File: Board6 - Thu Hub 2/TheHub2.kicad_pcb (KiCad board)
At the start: 2 copper layers, 53.3 x 127 mm, 31 parts, among them J1 12V Power, J2 SERVO, J3 I2C, U1 BNO055-Breakout, U2 FeatherM0, U3 RFM95-Breakout, U4 AZ1117-3.3, U5 L7806, U6 GT-U7_GPS, U7 MPL3115A2-Breakout

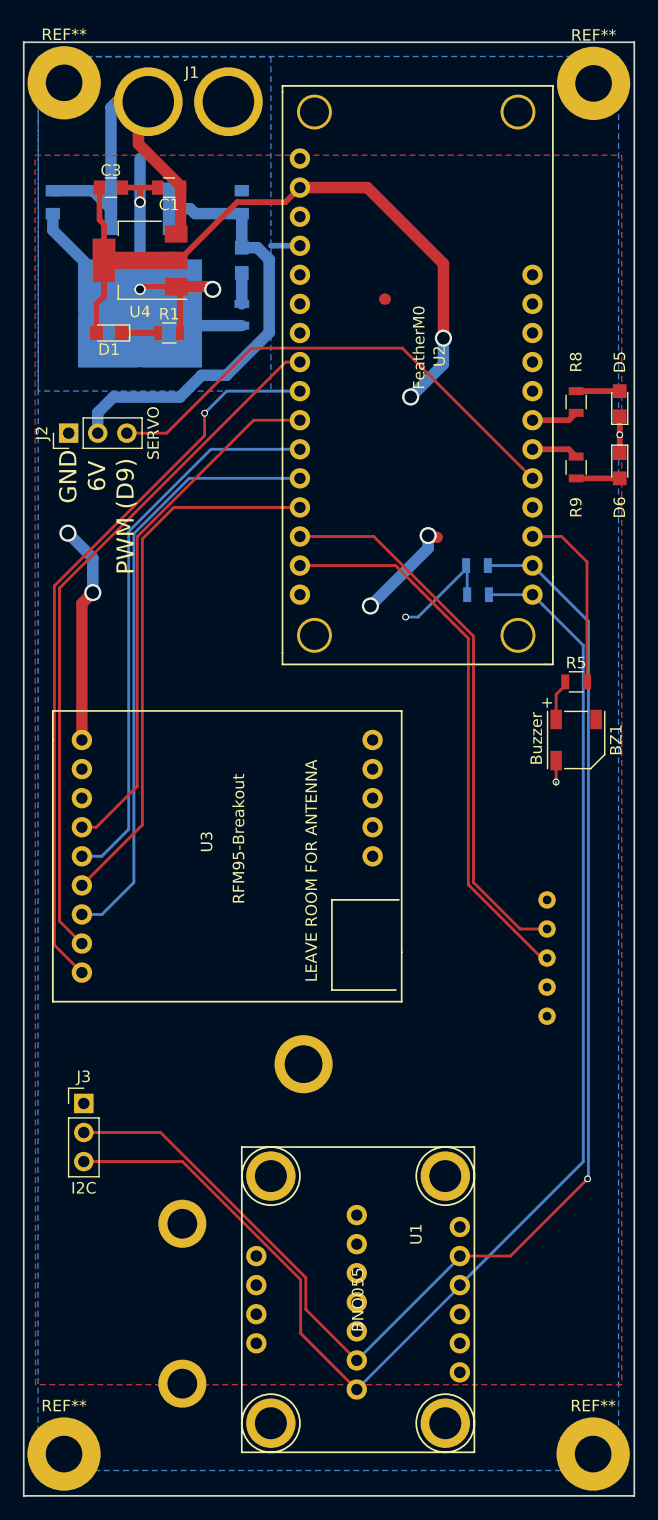
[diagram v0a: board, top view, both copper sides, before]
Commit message: For Hub2: add servo2 and GPS changed to breakout for MAX M8Q
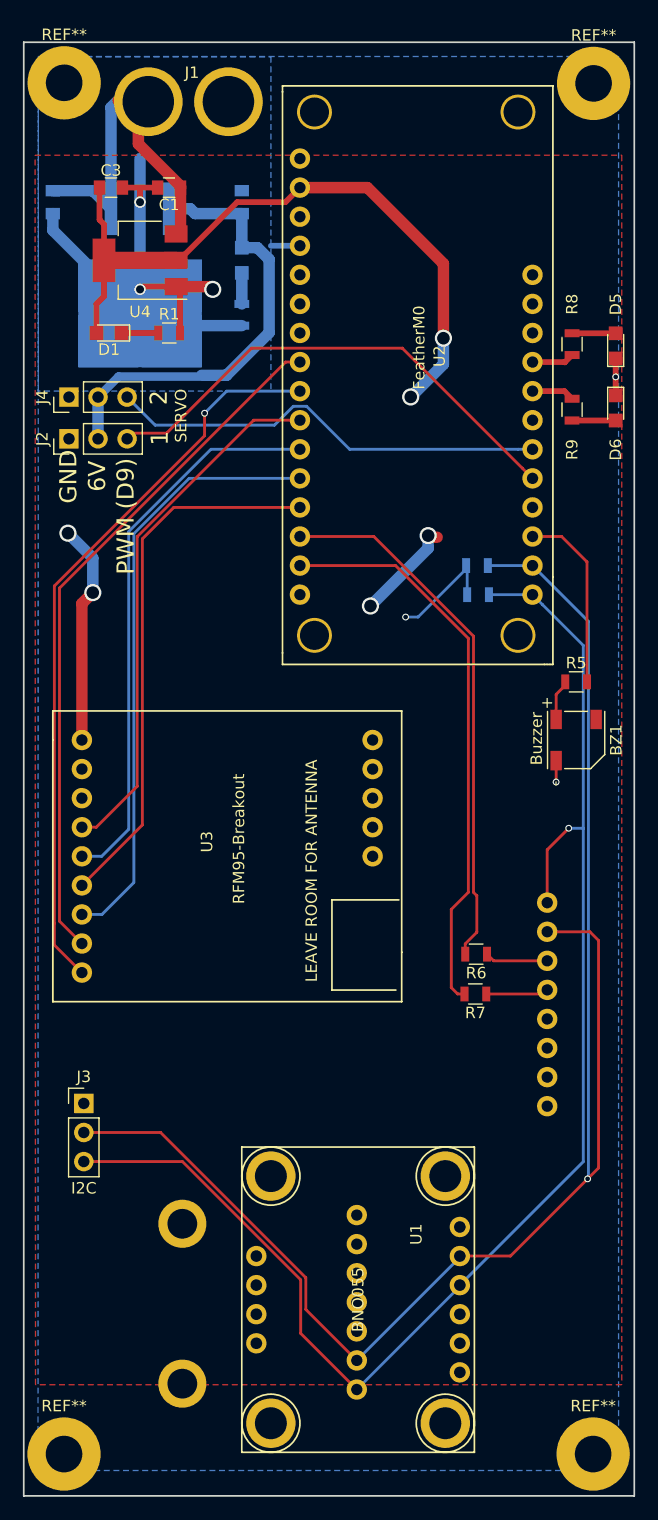
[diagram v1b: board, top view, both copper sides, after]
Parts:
- added J4: SERVO, Pin_Headers:Pin_Header_Straight_1x03_Pitch2.54mm, F.Cu at (103.0, 122.4)
- added R6: 0, Resistors_SMD:R_0805, F.Cu at (138.6, 171.1)
- added R7: 0, Resistors_SMD:R_0805, F.Cu at (138.5, 174.6)
- U6: value GT-U7_GPS -> MAX-M8Q-Breakout; footprint DannysLib:GPS_GT-07 -> DannysLib:MAX-M8Q-Breakout
- moved R8 5.07 mm to (147.0, 117.8)
- moved R9 5.07 mm to (147.0, 123.5)
- moved D5 5.07 mm to (150.8, 118.0)
- moved D6 5.07 mm to (150.8, 123.4)
- moved J2 0.50 mm to (103.0, 126.1)
- moved U6 0.24 mm to (144.8, 166.6), turned to 270 degrees
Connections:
- net /SERVO_PWM renamed /SERVO1_PWM
- U2 pad 22: /TEST_LED_2 -> /SERVO2_PWM
- U2 pad 23: /TEST_LED_1 -> Net-(U2-Pad23)
- U2 pad 24: Net-(U2-Pad24) -> /TEST_LED_2
- U2 pad 25: Net-(U2-Pad25) -> /TEST_LED_1
- U6 pad 1: Net-(U6-Pad1) -> /SDA
- U6 pad 2: /GPS_RX -> /SCL
- U6 pad 3: /GPS_TX -> Net-(R6-Pad1)
- U6 pad 4: GND -> Net-(R7-Pad1)
- U6 pad 5: +3V3 -> Net-(U6-Pad5)
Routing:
- net /SERVO2_PWM: track 0.00 -> 38.7 mm
- net /SCL: track 119.9 -> 145.9 mm
- net /SDA: track 118.1 -> 126.7 mm, vias 0 -> 1
- net Net-(R6-Pad1): track 0.00 -> 5.96 mm
- net Net-(R7-Pad1): track 0.00 -> 5.47 mm
- net /GPS_TX: track 48.4 -> 49.9 mm
- net /GPS_RX: track 48.4 -> 47.1 mm
- net /6V: track 38.4 -> 39.2 mm
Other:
- board text added: "1"
- board text added: "2"
